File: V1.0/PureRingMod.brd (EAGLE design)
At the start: 99 x 58.1 mm, 33 parts, among them IC1 TL074P, IC2 TL072P, X1 NC3FD-V

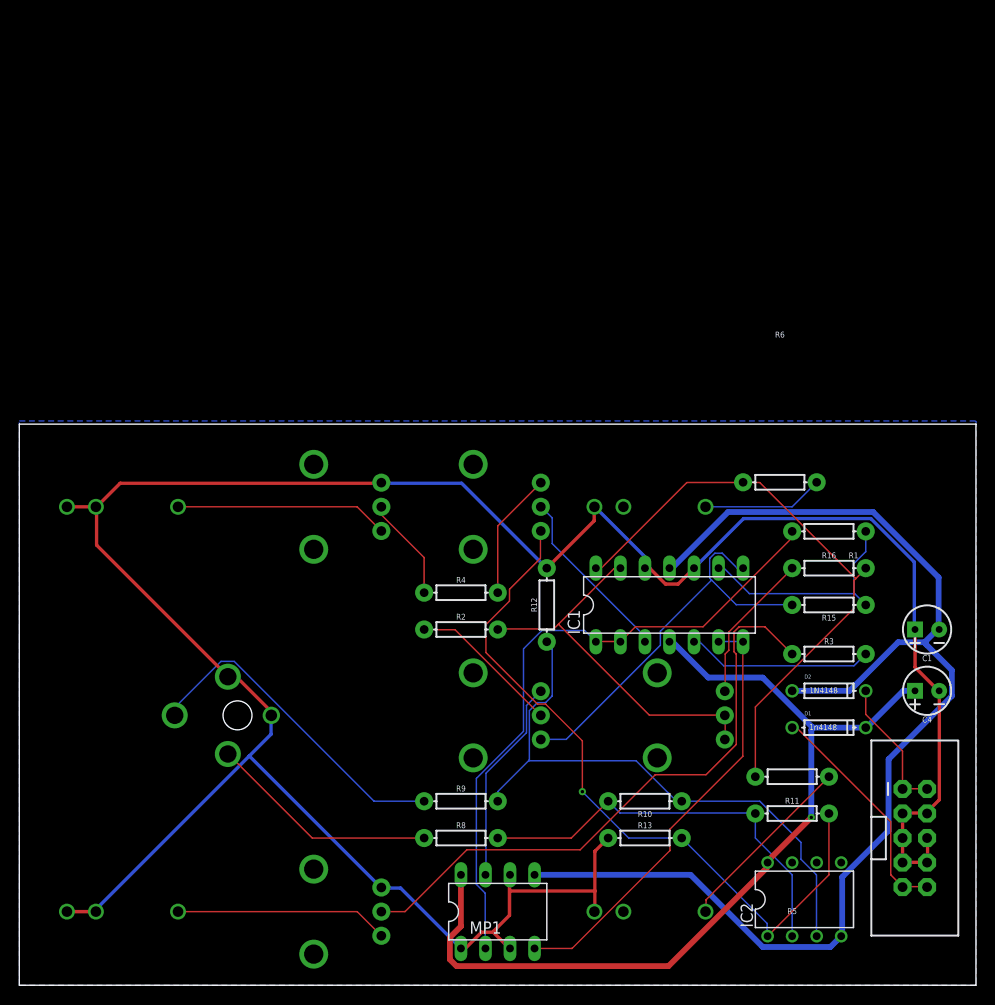
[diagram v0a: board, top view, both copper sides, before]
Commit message: Panel layout and routing
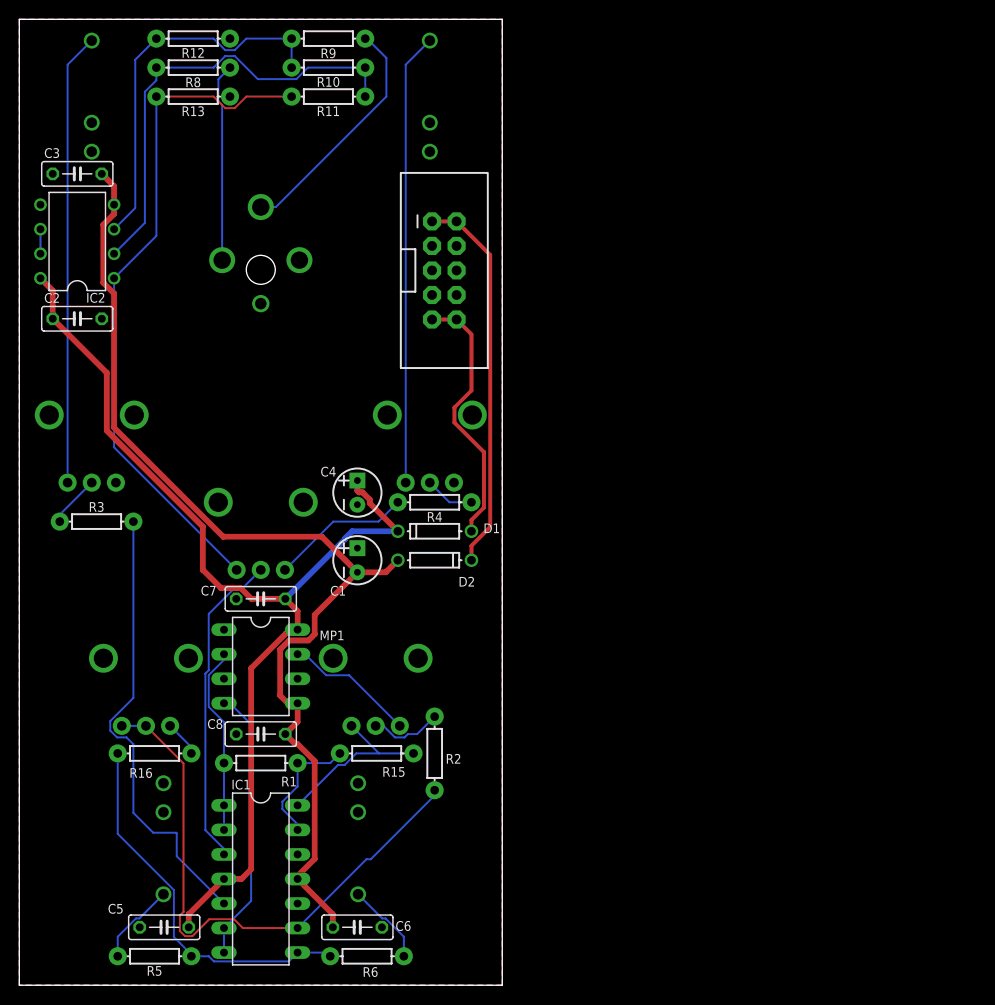
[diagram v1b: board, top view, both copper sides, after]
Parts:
- added C2, C3, C5, C6, C7, C8: (no value), PureRingMod:C050-025X075
- C1, C4: device SparkFun-Capacitors:CPOL-RADIAL-2.5MM-5MM -> PureRingMod:CPOL-RADIAL-2.5MM-5MM
- CARRIER, MODULATOR, OUTPUT: value (none) -> JACK; device INSTRUO:S_JACK -> PureRingMod:JACK
- D1, D2: device adafruit:DO-1N4148 -> PureRingMod:DO-1N4148
- GAIN, MICMIX, MIX, VOLCARIER, VOLMOD: device GMSN:POT -> PureRingMod:POT
- IC1: device GMSN:DIL14 -> PureRingMod:DIL14
- IC2: device GMSN-R2Project:DIL08 -> PureRingMod:DIL08
- MP1: value AD633AN -> AD633-2_AD633AN; device ad633-2:DIL08 -> PureRingMod:AD633-2_DIL08
- OUTPUT2: device INSTRUO:S_JACK -> PureRingMod:JACK
- POWER: device SparkFun-Connectors:2X5-SHROUDED -> PureRingMod:2X5-SHROUDED
- R1: value 100K -> 330; device SparkFun-Resistors:AXIAL-0.3 -> PureRingMod:AXIAL-0.3
- R10: value 27K -> 330; device SparkFun-Resistors:AXIAL-0.3 -> PureRingMod:AXIAL-0.3
- R11, R12: value 1M -> 330; device SparkFun-Resistors:AXIAL-0.3 -> PureRingMod:AXIAL-0.3
- R13, R16, R2: value 10K -> 330; device SparkFun-Resistors:AXIAL-0.3 -> PureRingMod:AXIAL-0.3
- R15: value 20K -> 330; device SparkFun-Resistors:AXIAL-0.3 -> PureRingMod:AXIAL-0.3
- R3, R4: value 4k7 -> 330; device SparkFun-Resistors:AXIAL-0.3 -> PureRingMod:AXIAL-0.3
- R5, R6: value 1K -> 330; device SparkFun-Resistors:AXIAL-0.3 -> PureRingMod:AXIAL-0.3
- R8, R9: device SparkFun-Resistors:AXIAL-0.3 -> PureRingMod:AXIAL-0.3
- X1: value NC3FD-V -> CON-NEUTRIK_AG_NC3FD-V; device con-neutrik_ag:NC3FD-V -> PureRingMod:CON-NEUTRIK_AG_NC3FD-V
- moved IC2 101.5 mm to (6.00, 77.0), turned to 90 degrees
- moved R13 89.9 mm to (18.0, 92.0), turned to 180 degrees
- moved R11 88.4 mm to (32.0, 92.0), turned to 180 degrees
- moved MODULATOR 85.3 mm to (7.50, 92.8), turned to 0 degrees
- moved R8 84.4 mm to (18.0, 95.0), turned to 180 degrees
- moved R10 82.7 mm to (32.0, 95.0), turned to 0 degrees
- moved R9 80.1 mm to (32.0, 98.0), turned to 180 degrees
- moved R3 77.0 mm to (8.00, 48.0)
- moved POWER 76.3 mm to (44.0, 74.0)
- moved R16 72.4 mm to (14.0, 24.0), turned to 180 degrees
- moved R12 69.1 mm to (18.0, 98.0), turned to 0 degrees
- moved R5 68.6 mm to (14.0, 3.00), turned to 180 degrees
- moved R6 65.1 mm to (36.0, 3.00)
- moved R1 63.5 mm to (25.0, 23.0)
- moved C4 62.4 mm to (35.0, 51.0), turned to 90 degrees
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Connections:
- new net N$13: IC2.6, IC2.7
- net +12V: now also C2.1, C5.1, C7.1
- net -12V: now also C3.2, C6.2, C8.2
- net GND: now also C2.2, C3.1, C5.2, C6.1, C7.2, C8.1, IC2.5
- net N$12: now also IC1.8; no longer IC1.14
- net N$14: now also IC1.13; no longer IC1.9
- net N$4: now also IC1.14; no longer IC1.8
- net N$7: now also IC1.9; no longer IC1.13
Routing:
- net GND: track 266.0 -> 0.00 mm
- net N$19: track 63.1 -> 5.40 mm
- net N$1: track 67.7 -> 19.5 mm
- net N$11: track 19.3 -> 47.4 mm
- net N$10: track 14.3 -> 39.9 mm
- net N$17: track 22.1 -> 46.8 mm
- net N$16: track 22.1 -> 46.8 mm
- net N$4: track 41.4 -> 18.3 mm
- net N$25: track 61.6 -> 39.5 mm
- net N$12: track 61.0 -> 39.4 mm
- net N$7: track 39.0 -> 59.4 mm
- net -12V: track 127.9 -> 110.6 mm
- net N$2: track 45.5 -> 28.5 mm
- net +12V: track 93.7 -> 109.5 mm, vias 1 -> 0
- net N$30: track 18.5 -> 33.1 mm
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- added copper zone on layer 1, net GND
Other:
- board size 99 x 58.1 mm -> 50 x 100 mm
- board text added: "Ring Modulator v1.1 cc-by-sa-4.0 Design Andy C From a design by Roman Sowa"
- board text removed: "CC BY 3.0"
- board text removed: "Ring Modulator Design Andy C From a design by Roman Sowa"
- board text removed: "V1.0"
